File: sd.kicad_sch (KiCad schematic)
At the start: 81 parts, among them J2 MicroSD_1140084168, J4 USB-C_GCT_USB4105-GF-A, J5 USB-A_UJ2-AH-4-SMT-TR, Q1 PJE138K, Q2 PJE138K, U1 USB2642_ML, U2 AP22615A_TSOT26, U3 AP22615A_TSOT26, U5 FUSB303B, Y2 Resonator_24MHz_ABM8G

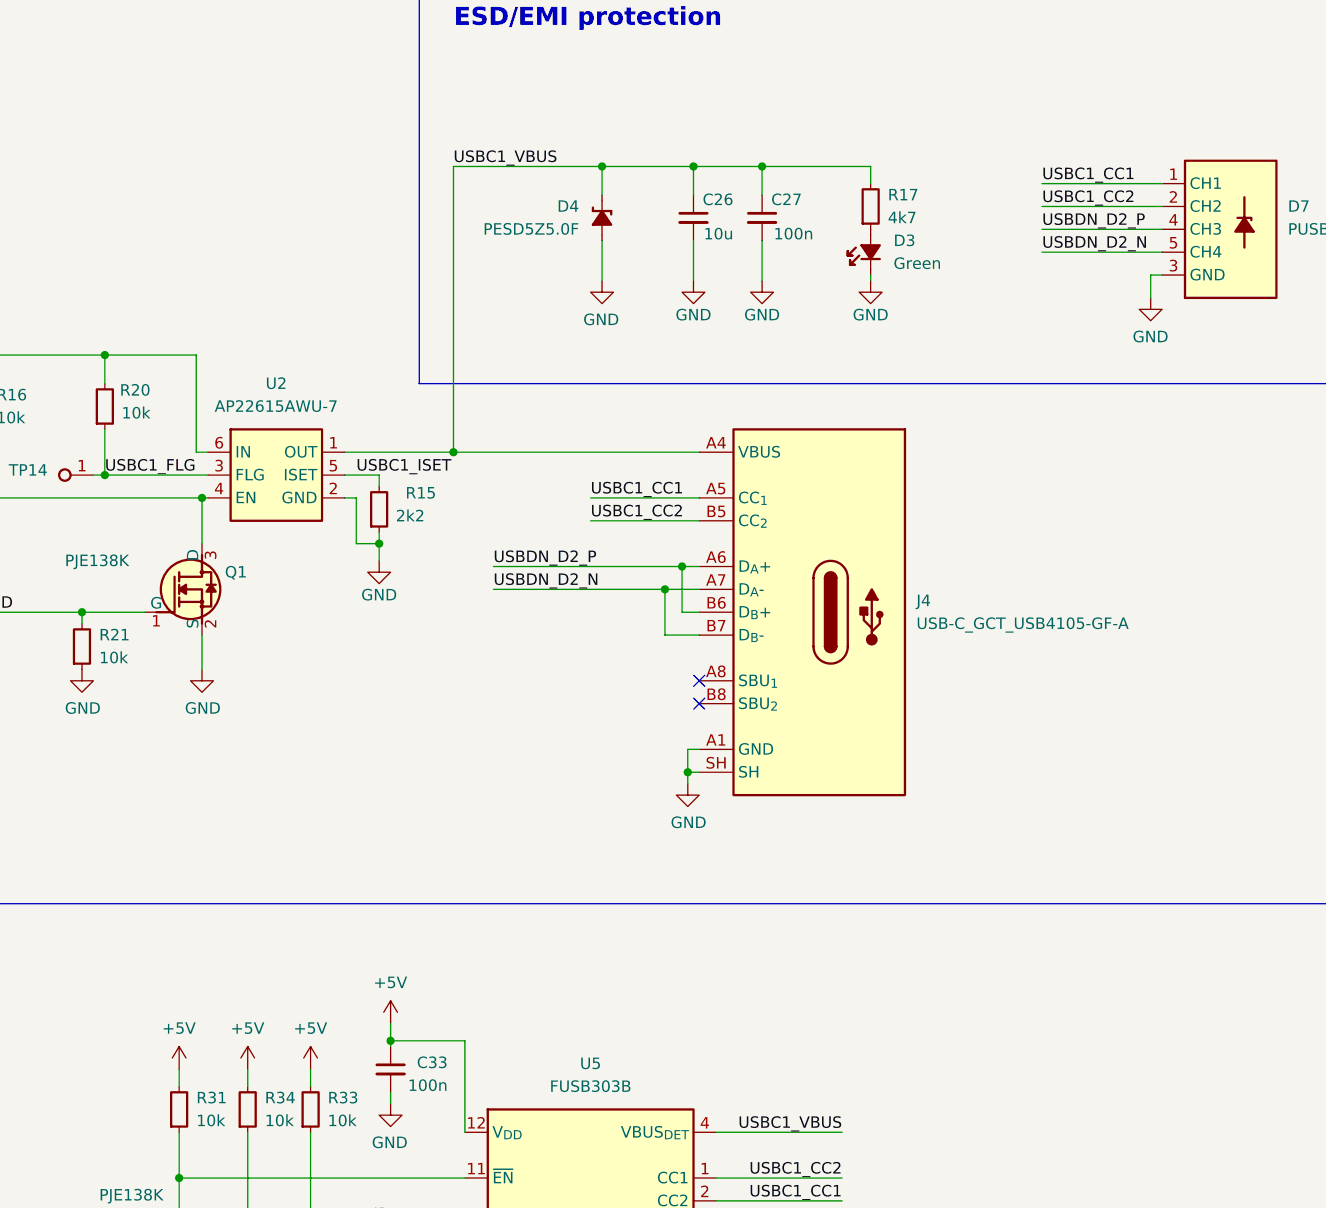
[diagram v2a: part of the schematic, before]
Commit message: [#64333] Continued routing components
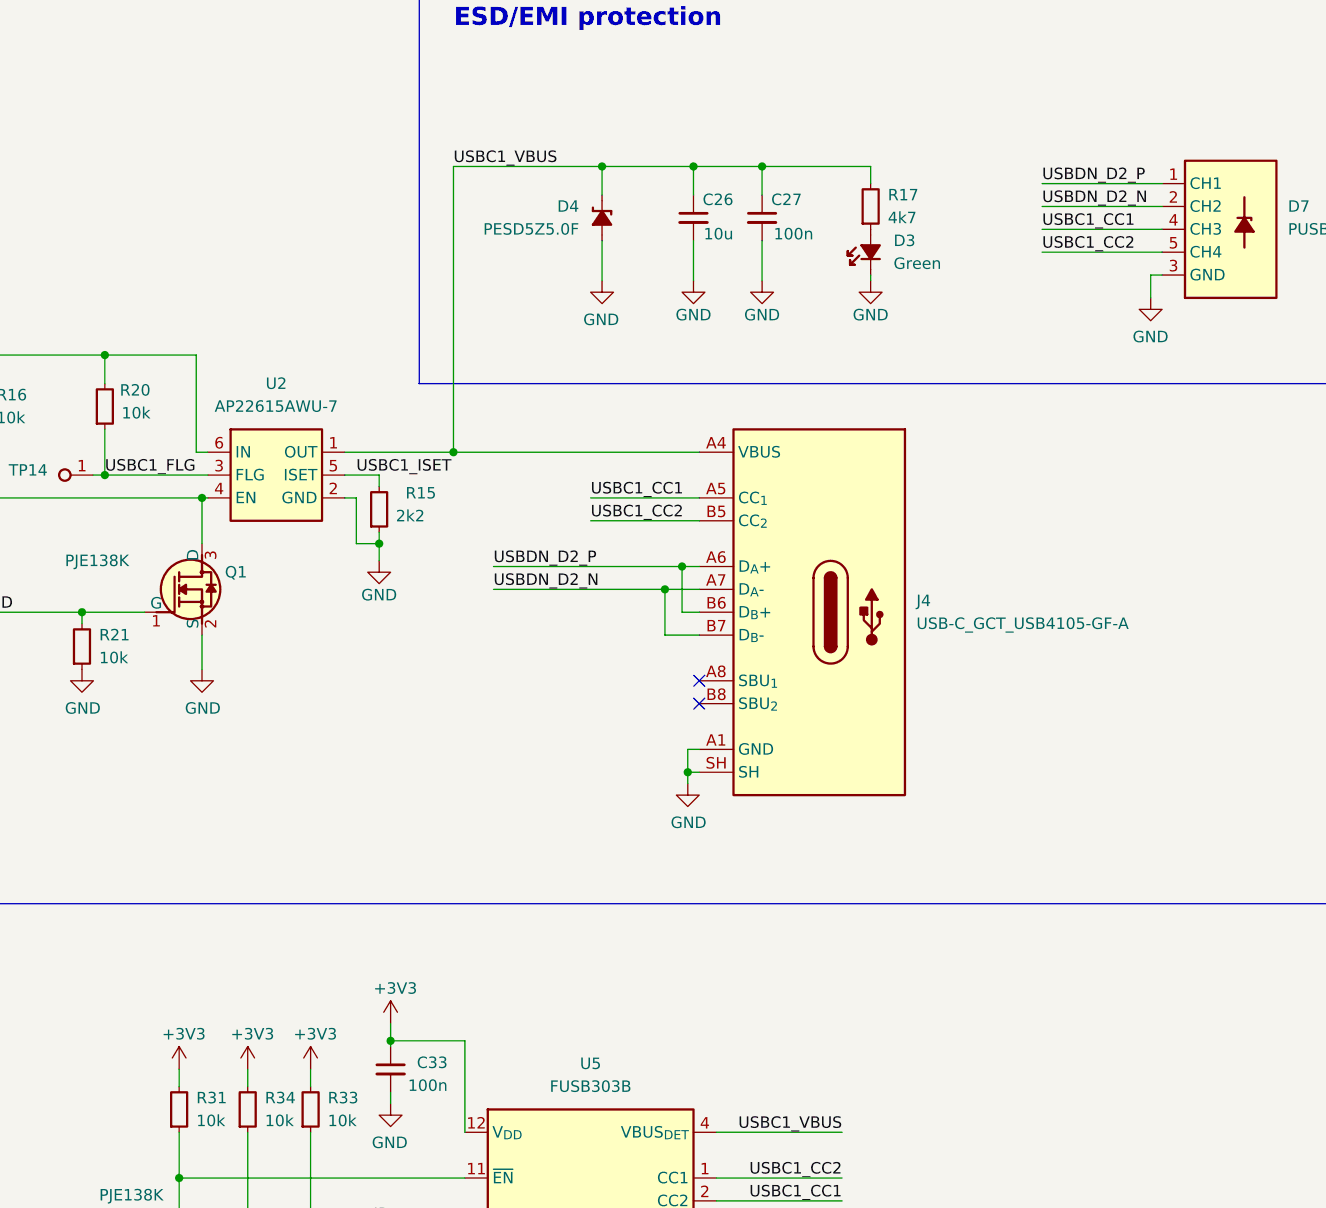
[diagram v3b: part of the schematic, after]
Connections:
- net +5V is gone; now on net +3V3: C33.1, R31.2, R33.2, R34.2, U5.12 (V_{DD})
- net USBC1_CC1: now also D7.4 (CH3), D7.7 (CH3); no longer D7.1 (CH1), D7.10 (CH1)
- net USBC1_CC2: now also D7.5 (CH4), D7.6 (CH4); no longer D7.2 (CH2), D7.9 (CH2)
- net USBDN_D2_N: now also D7.2 (CH2), D7.9 (CH2); no longer D7.5 (CH4), D7.6 (CH4)
- net USBDN_D2_P: now also D7.1 (CH1), D7.10 (CH1); no longer D7.4 (CH3), D7.7 (CH3)
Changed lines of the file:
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@@
     (stroke (width 0) (type default))
   )
-  (wire (pts (xy 353.695 40.64) (xy 367.03 40.64))
+  (wire (pts (xy 353.695 35.56) (xy 367.03 35.56))
     (stroke (width 0) (type default))
   )
@@
     (stroke (width 0) (type default))
   )
-  (wire (pts (xy 353.695 35.56) (xy 367.03 35.56))
+  (wire (pts (xy 353.695 40.64) (xy 367.03 40.64))
     (stroke (width 0) (type default))
   )
@@
     (stroke (width 0) (type default))
   )
-  (wire (pts (xy 353.695 38.1) (xy 367.03 38.1))
+  (wire (pts (xy 353.695 43.18) (xy 367.03 43.18))
     (stroke (width 0) (type default))
   )
@@
     (stroke (width 0) (type default))
   )
-  (wire (pts (xy 353.695 43.18) (xy 367.03 43.18))
+  (wire (pts (xy 353.695 38.1) (xy 367.03 38.1))
     (stroke (width 0) (type default))
   )
@@
     (effects (font (size 1.27 1.27)) (justify left bottom))
   )
-  (label "USBDN_D2_P" (at 353.695 40.64 0) (fields_autoplaced)
+  (label "USBDN_D2_P" (at 353.695 35.56 0) (fields_autoplaced)
     (effects (font (size 1.27 1.27)) (justify left bottom))
   )
@@
     (effects (font (size 1.27 1.27)) (justify left bottom))
   )
-  (label "USBC1_CC2" (at 353.695 38.1 0) (fields_autoplaced)
+  (label "USBC1_CC2" (at 353.695 43.18 0) (fields_autoplaced)
     (effects (font (size 1.27 1.27)) (justify left bottom))
   )
@@
     (effects (font (size 1.27 1.27)) (justify right bottom))
   )
-  (label "USBDN_D2_N" (at 353.695 43.18 0) (fields_autoplaced)
+  (label "USBDN_D2_N" (at 353.695 38.1 0) (fields_autoplaced)
     (effects (font (size 1.27 1.27)) (justify left bottom))
   )
@@
     (effects (font (size 1.27 1.27)) (justify right bottom))
   )
-  (label "USBC1_CC1" (at 353.695 35.56 0) (fields_autoplaced)
+  (label "USBC1_CC1" (at 353.695 40.64 0) (fields_autoplaced)
     (effects (font (size 1.27 1.27)) (justify left bottom))
   )
@@
     )
   )
-  (symbol (lib_id "antmicropower:+5V") (at 257.81 133.985 0) (unit 1)
-    (in_bom yes) (on_board yes) (dnp no)
-    (property "Reference" "#PWR061" (at 257.81 137.795 0)
-      (effects (font (size 1.27 1.27)) (justify left bottom) hide)
-    )
-    (property "Value" "+5V" (at 255.905 130.175 0)
-      (effects (font (size 1.27 1.27)) (justify left bottom))
-    )
-    (property "Footprint" "" (at 257.81 133.985 0)
-      (effects (font (size 1.27 1.27)) (justify left bottom) hide)
-    )
-    (property "Datasheet" "" (at 257.81 133.985 0)
-      (effects (font (size 1.27 1.27)) (justify left bottom) hide)
-    )
-    (pin "1")
-    (instances
-      (project "jetson-orin-baseboard-storage-expansion"
-        (path "/45f331f1-15bc-4fff-94ad-9fb3699b0151/73e7794c-25e6-4d08-8054-2f71767fcb84"
-          (reference "#PWR061") (unit 1)
-        )
-      )
-    )
-  )
   (symbol (lib_id "antmicroTestPoints:TP_0.75mm_SMD") (at 68.58 114.3 180) (unit 1)
     (in_bom no) (on_board yes) (dnp no)
@@
     )
   )
-  (symbol (lib_id "antmicropower:+5V") (at 272.415 133.985 0) (unit 1)
-    (in_bom yes) (on_board yes) (dnp no)
-    (property "Reference" "#PWR063" (at 272.415 137.795 0)
-      (effects (font (size 1.27 1.27)) (justify left bottom) hide)
-    )
-    (property "Value" "+5V" (at 270.51 130.175 0)
-      (effects (font (size 1.27 1.27)) (justify left bottom))
-    )
-    (property "Footprint" "" (at 272.415 133.985 0)
-      (effects (font (size 1.27 1.27)) (justify left bottom) hide)
-    )
-    (property "Datasheet" "" (at 272.415 133.985 0)
-      (effects (font (size 1.27 1.27)) (justify left bottom) hide)
-    )
-    (pin "1")
-    (instances
-      (project "jetson-orin-baseboard-storage-expansion"
-        (path "/45f331f1-15bc-4fff-94ad-9fb3699b0151/73e7794c-25e6-4d08-8054-2f71767fcb84"
-          (reference "#PWR063") (unit 1)
-        )
-      )
-    )
-  )
   (symbol (lib_id "antmicroLEDIndicationDiscrete:LED_G_0603_LTST-C190GKT") (at 334.645 45.72 90) (unit 1)
     (in_bom yes) (on_board yes) (dnp no) (fields_autoplaced)
@@
     )
   )
+  (symbol (lib_id "antmicropower:+3V3") (at 272.415 133.985 0) (unit 1)
+    (in_bom yes) (on_board yes) (dnp no)
+    (property "Reference" "#PWR054" (at 272.415 137.795 0)
+      (effects (font (size 1.27 1.27)) hide)
+    )
+    (property "Value" "+3V3" (at 270.51 130.81 0)
+      (effects (font (size 1.27 1.27)) (justify left bottom))
+    )
+    (property "Footprint" "" (at 272.415 133.985 0)
+      (effects (font (size 1.27 1.27)) hide)
+    )
+    (property "Datasheet" "" (at 272.415 133.985 0)
+      (effects (font (size 1.27 1.27)) hide)
+    )
+    (pin "1")
+    (instances
+      (project "jetson-orin-baseboard-storage-expansion"
+        (path "/45f331f1-15bc-4fff-94ad-9fb3699b0151/73e7794c-25e6-4d08-8054-2f71767fcb84"
+          (reference "#PWR054") (unit 1)
+        )
+      )
+    )
+  )
   (symbol (lib_id "antmicroCapacitors0402:C_4u7_0402") (at 59.69 43.18 270) (mirror x) (unit 1)
     (in_bom yes) (on_board yes) (dnp no)
@@
     )
   )
+  (symbol (lib_id "antmicropower:+3V3") (at 257.81 133.985 0) (unit 1)
+    (in_bom yes) (on_board yes) (dnp no)
+    (property "Reference" "#PWR052" (at 257.81 137.795 0)
+      (effects (font (size 1.27 1.27)) hide)
+    )
+    (property "Value" "+3V3" (at 255.905 130.81 0)
+      (effects (font (size 1.27 1.27)) (justify left bottom))
+    )
+    (property "Footprint" "" (at 257.81 133.985 0)
+      (effects (font (size 1.27 1.27)) hide)
+    )
+    (property "Datasheet" "" (at 257.81 133.985 0)
+      (effects (font (size 1.27 1.27)) hide)
+    )
+    (pin "1")
+    (instances
+      (project "jetson-orin-baseboard-storage-expansion"
+        (path "/45f331f1-15bc-4fff-94ad-9fb3699b0151/73e7794c-25e6-4d08-8054-2f71767fcb84"
+          (reference "#PWR052") (unit 1)
+        )
+      )
+    )
+  )
   (symbol (lib_id "antmicroResistors0402:R_4k7_0402") (at 172.72 96.52 90) (unit 1)
     (in_bom yes) (on_board yes) (dnp no) (fields_autoplaced)
@@
     )
   )
+  (symbol (lib_id "antmicropower:+3V3") (at 265.43 133.985 0) (unit 1)
+    (in_bom yes) (on_board yes) (dnp no)
+    (property "Reference" "#PWR053" (at 265.43 137.795 0)
+      (effects (font (size 1.27 1.27)) hide)
+    )
+    (property "Value" "+3V3" (at 263.525 130.81 0)
+      (effects (font (size 1.27 1.27)) (justify left bottom))
+    )
+    (property "Footprint" "" (at 265.43 133.985 0)
+      (effects (font (size 1.27 1.27)) hide)
+    )
+    (property "Datasheet" "" (at 265.43 133.985 0)
+      (effects (font (size 1.27 1.27)) hide)
+    )
+    (pin "1")
+    (instances
+      (project "jetson-orin-baseboard-storage-expansion"
+        (path "/45f331f1-15bc-4fff-94ad-9fb3699b0151/73e7794c-25e6-4d08-8054-2f71767fcb84"
+          (reference "#PWR053") (unit 1)
+        )
+      )
+    )
+  )
   (symbol (lib_id "antmicroCapacitors0402:C_100n_0402") (at 226.695 55.88 90) (mirror x) (unit 1)
     (in_bom yes) (on_board yes) (dnp no)
@@
     )
   )
-  (symbol (lib_id "antmicropower:+5V") (at 265.43 133.985 0) (unit 1)
-    (in_bom yes) (on_board yes) (dnp no)
-    (property "Reference" "#PWR065" (at 265.43 137.795 0)
-      (effects (font (size 1.27 1.27)) (justify left bottom) hide)
-    )
-    (property "Value" "+5V" (at 263.525 130.175 0)
-      (effects (font (size 1.27 1.27)) (justify left bottom))
-    )
-    (property "Footprint" "" (at 265.43 133.985 0)
-      (effects (font (size 1.27 1.27)) (justify left bottom) hide)
-    )
-    (property "Datasheet" "" (at 265.43 133.985 0)
-      (effects (font (size 1.27 1.27)) (justify left bottom) hide)
-    )
-    (pin "1")
-    (instances
-      (project "jetson-orin-baseboard-storage-expansion"
-        (path "/45f331f1-15bc-4fff-94ad-9fb3699b0151/73e7794c-25e6-4d08-8054-2f71767fcb84"
-          (reference "#PWR065") (unit 1)
-        )
-      )
-    )
-  )
   (symbol (lib_id "antmicroTestPoints:TP_0.75mm_SMD") (at 289.56 161.29 0) (mirror y) (unit 1)
     (in_bom no) (on_board yes) (dnp no)
@@
     )
   )
-  (symbol (lib_id "antmicropower:+5V") (at 281.305 128.905 0) (unit 1)
-    (in_bom yes) (on_board yes) (dnp no)
-    (property "Reference" "#PWR057" (at 281.305 132.715 0)
-      (effects (font (size 1.27 1.27)) (justify left bottom) hide)
-    )
-    (property "Value" "+5V" (at 279.4 125.095 0)
-      (effects (font (size 1.27 1.27)) (justify left bottom))
-    )
-    (property "Footprint" "" (at 281.305 128.905 0)
-      (effects (font (size 1.27 1.27)) (justify left bottom) hide)
-    )
-    (property "Datasheet" "" (at 281.305 128.905 0)
-      (effects (font (size 1.27 1.27)) (justify left bottom) hide)
-    )
-    (pin "1")
-    (instances
-      (project "jetson-orin-baseboard-storage-expansion"
-        (path "/45f331f1-15bc-4fff-94ad-9fb3699b0151/73e7794c-25e6-4d08-8054-2f71767fcb84"
-          (reference "#PWR057") (unit 1)
-        )
-      )
-    )
-  )
   (symbol (lib_id "antmicropower:GND") (at 307.34 212.09 0) (mirror y) (unit 1)
     (in_bom yes) (on_board yes) (dnp no)
@@
         )
       )
+    )
+  )
+  (symbol (lib_id "antmicropower:+3V3") (at 281.305 128.905 0) (unit 1)
+    (in_bom yes) (on_board yes) (dnp no)
+    (property "Reference" "#PWR056" (at 281.305 132.715 0)
+      (effects (font (size 1.27 1.27)) hide)
+    )
+    (property "Value" "+3V3" (at 279.4 125.73 0)
+      (effects (font (size 1.27 1.27)) (justify left bottom))
+    )
+    (property "Footprint" "" (at 281.305 128.905 0)
+      (effects (font (size 1.27 1.27)) hide)
+    )
+    (property "Datasheet" "" (at 281.305 128.905 0)
+      (effects (font (size 1.27 1.27)) hide)
+    )
+    (pin "1")
+    (instances
+      (project "jetson-orin-baseboard-storage-expansion"
+        (path "/45f331f1-15bc-4fff-94ad-9fb3699b0151/73e7794c-25e6-4d08-8054-2f71767fcb84"
+          (reference "#PWR056") (unit 1)
+        )
+      )
